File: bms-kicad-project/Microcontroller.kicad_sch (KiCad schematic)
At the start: 49 parts, among them J3 12402012E212A, J4 DEBUG, J5 Conn_02x20_Counter_Clockwise, Q13 BSS308PE_H6327, SW1 KMR223G LFG, SW2 KMR223G LFG, U3 W25Q128JVSIQ TR, U4 NCP1117ST33T3G, U5 RP2040, X1 ABM8-272-T3

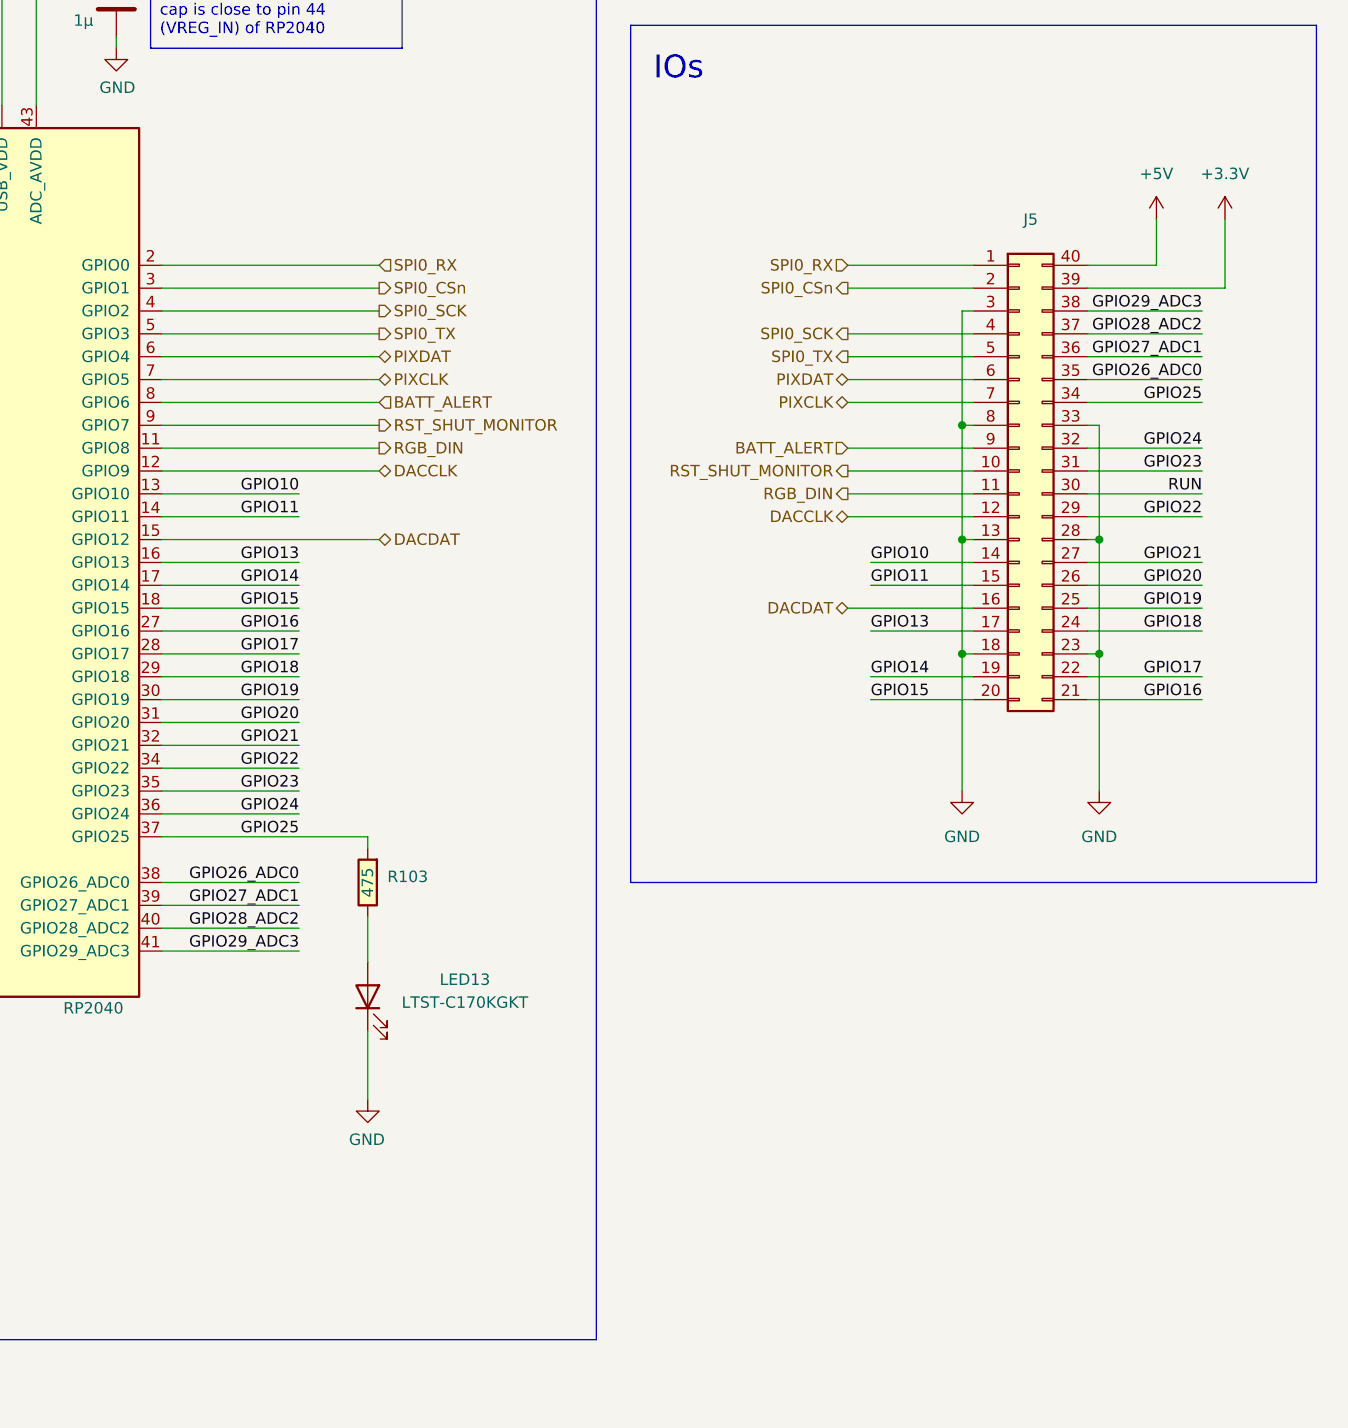
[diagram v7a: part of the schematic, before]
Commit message: feat: Added temp sensors
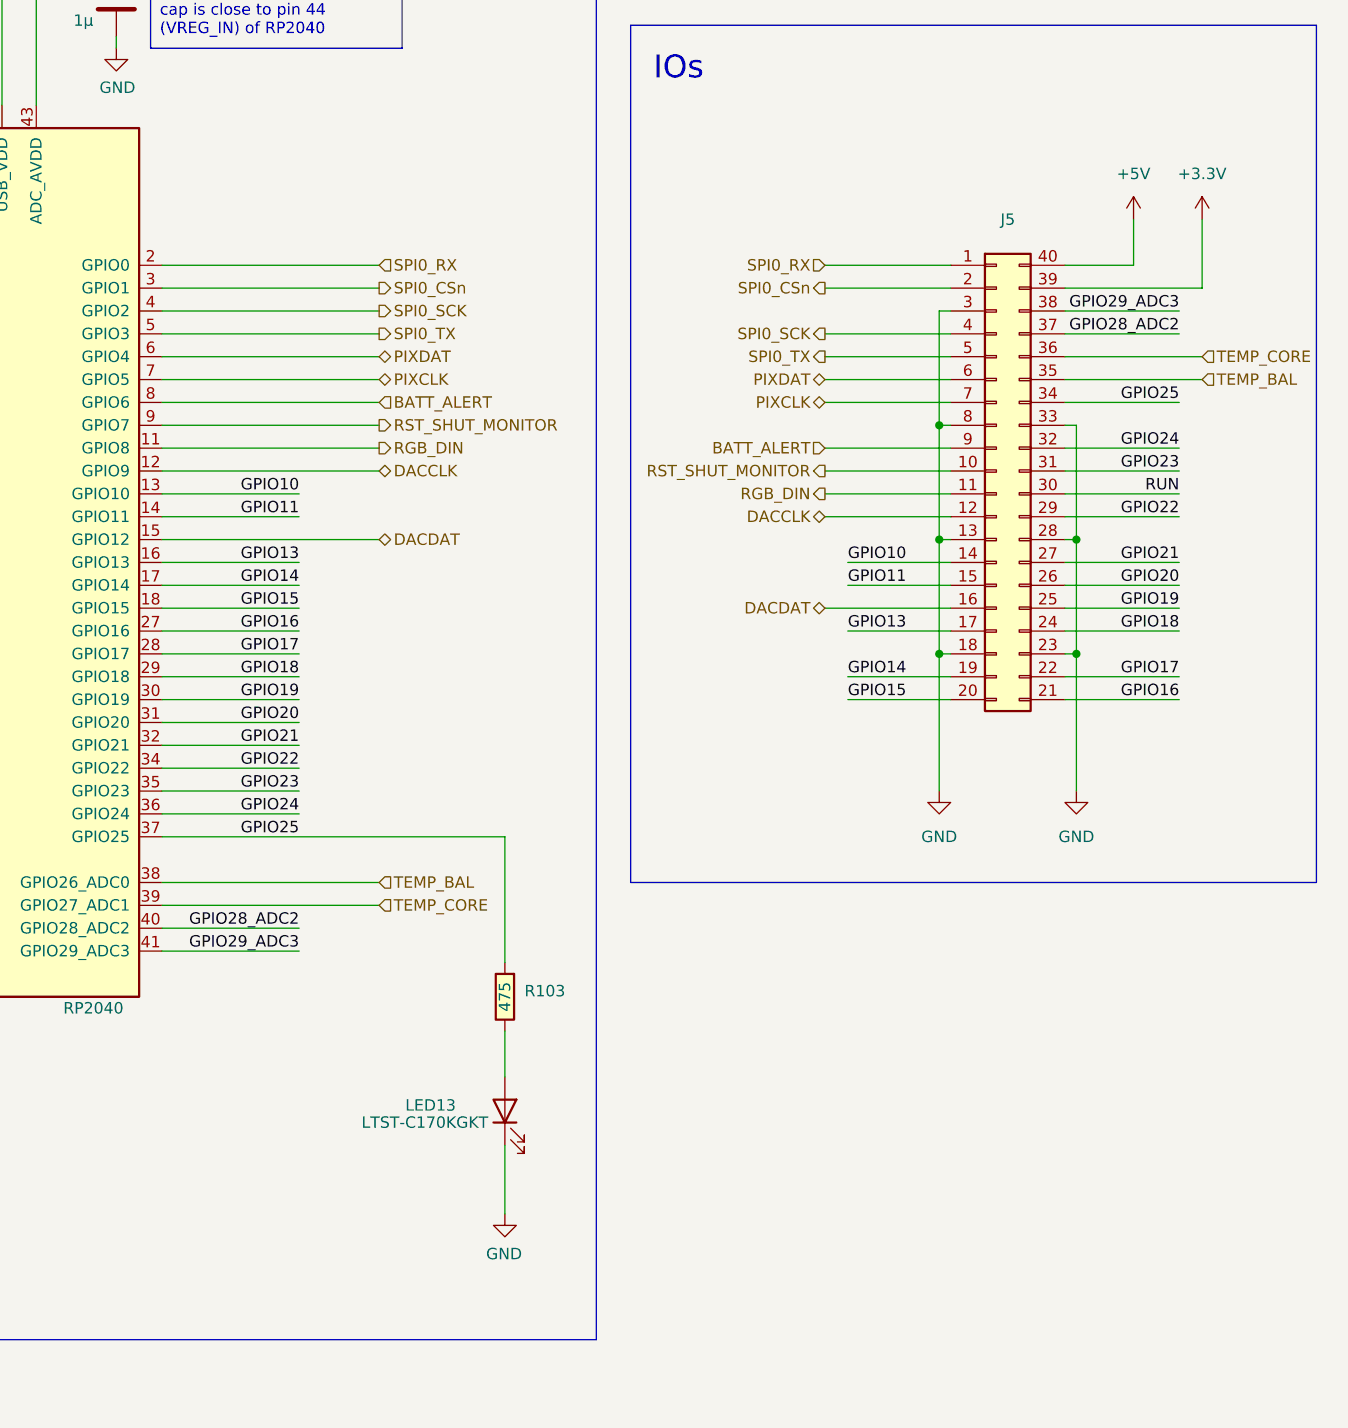
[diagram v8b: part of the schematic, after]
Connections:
- net GPIO26_ADC0 renamed TEMP_BAL
- net GPIO27_ADC1 renamed TEMP_CORE
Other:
- moved on the sheet: J5, LED13, R103
